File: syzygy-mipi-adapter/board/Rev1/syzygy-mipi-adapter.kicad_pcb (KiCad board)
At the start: 4 copper layers, 45 x 70 mm, 98 parts, among them J1 Conn_02x06_Odd_Even, J2 SYZYGY_STD, J3 USB_C_Receptacle_USB2.0_16P, J4 SM03B-SRSS-TB, J6 501951-2230, J7 501951-2230, J8 501951-2230, Q1 DMG1024UV-7, Q2 DMG1024UV-7, U1 RP2350_80QFN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

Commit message: Consolidate footprints from several footprint libraries into CUSTOM.pretty
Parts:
- J6, J7, J8: footprint FPC:501951-2230 -> CUSTOM:501951-2230
- L1: footprint RP2350_60QFN_minimal:L_pol_2016 -> CUSTOM:L_pol_2016
- U1: footprint RP2350_60QFN_minimal:RP2350B_QFN-80_EP_10.573x10.573_Pitch0.4mm -> CUSTOM:RP2350B_QFN-80_EP_10.573x10.573_Pitch0.4mm
- U10, U3, U4, U5, U6, U7, U8, U9: footprint FPC:PUSB3F96X -> CUSTOM:PUSB3F96X

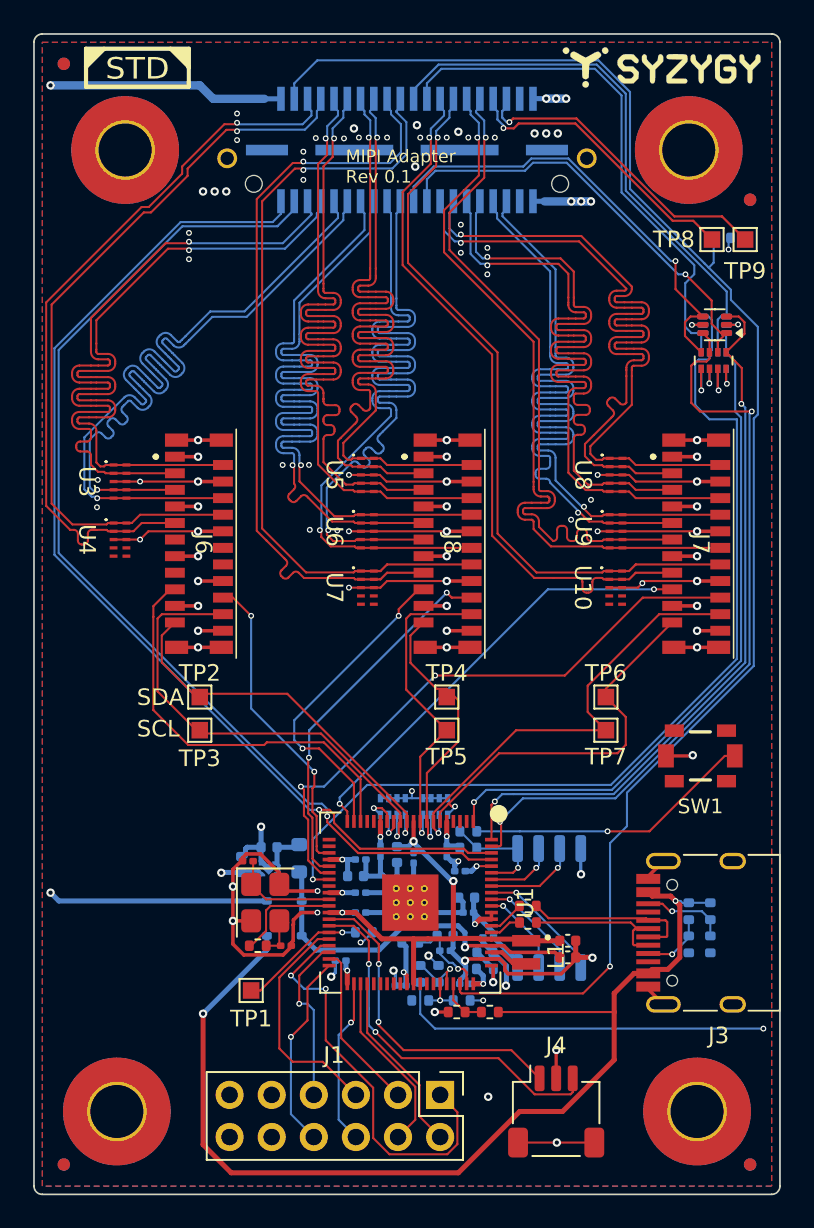
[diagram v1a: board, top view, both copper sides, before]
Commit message: Fix issue #5 as described in that issue
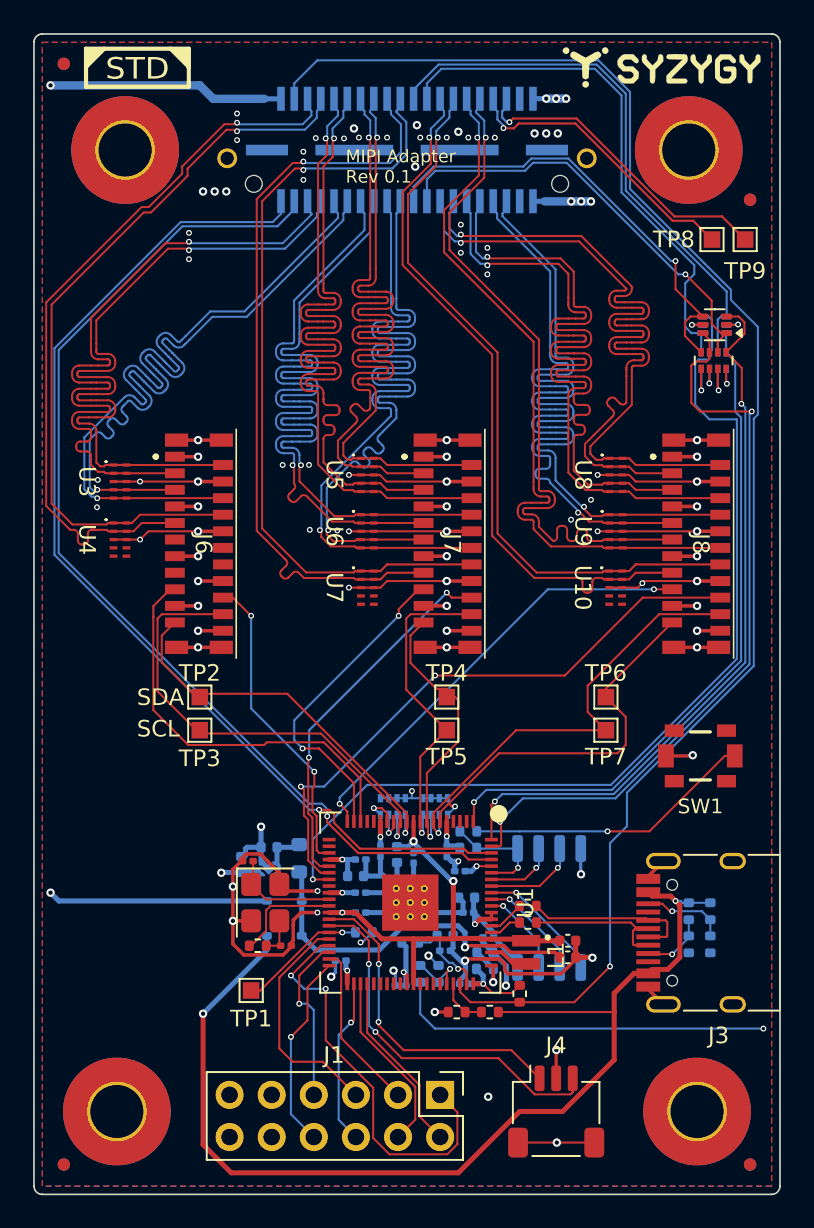
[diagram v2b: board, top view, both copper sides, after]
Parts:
- removed R10: 10K, Resistor_SMD:R_0402_1005Metric
- removed R11: 56K, Resistor_SMD:R_0402_1005Metric
- R18: moved to F.Cu
- moved R18 47.2 mm to (129.3, 117.9), turned to 90 degrees
- renumbered J8 to J7, J7 to J8
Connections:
- R18 pad 2: P3V3D -> PMCUD
- U1 pad 55: Net-(U1-GPIO44_ADC4) -> unconnected-(U1-GPIO44_ADC4-Pad55)
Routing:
- net PMCUD: track 28.8 -> 31.4 mm
- net Net-(U1-GPIO44_ADC4): track 2.48 -> 0.00 mm, vias 1 -> 0
- net P3V3D: track 16.1 -> 14.5 mm, vias 11 -> 9
- net /R_GA: track 94.9 -> 93.4 mm

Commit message: Fix issue #7
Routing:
- net P5VD: track 27.5 -> 32.8 mm
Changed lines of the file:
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@@
 	)
 	(via
-		(at 101 63.1)
+		(at 101 72.4)
 		(size 0.508)
 		(drill 0.254)
@@
 	)
 	(segment
-		(start 110.81 63.91)
-		(end 110 63.1)
+		(start 113.9 63.91)
+		(end 110.69 63.91)
 		(width 0.508)
 		(layer "B.Cu")
@@
 	)
 	(segment
-		(start 110 63.1)
-		(end 101 63.1)
+		(start 110.69 63.91)
+		(end 109.9 64.7)
+		(width 0.508)
+		(layer "B.Cu")
+		(net 1)
+	)
+	(segment
+		(start 109.9 64.7)
+		(end 109.9 68.4)
 		(width 0.508)
 		(layer "B.Cu")
@@
 	)
 	(segment
-		(start 113.9 63.91)
-		(end 110.81 63.91)
+		(start 109.9 68.4)
+		(end 105.9 72.4)
 		(width 0.508)
 		(layer "B.Cu")
+		(net 1)
+	)
+	(segment
+		(start 105.9 72.4)
+		(end 101 72.4)
+		(width 0.508)
+		(layer "B.Cu")

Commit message: Fix issue #6 and other silkscreen issues. Moved I2C test points a bit further away from FPCs.
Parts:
- moved TP4 5.81 mm to (119.1, 99.6)
- moved TP5 5.81 mm to (119.1, 101.6)
- moved TP2 5.32 mm to (115.3, 99.6)
- moved TP3 5.32 mm to (115.3, 101.6)
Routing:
- net /SCL1: track 20.1 -> 24.9 mm
- net /SDA1: track 17.0 -> 18.6 mm
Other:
- board text added: "MIPI Adapter Rev 1"
- board text added: "MIPI0"
- board text added: "MIPI1"
- board text added: "MIPI2"
- board text removed: "MIPI Adapter Rev 0.1"
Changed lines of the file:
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@@
 			(at 0.2 -1.8 270)
 			(layer "F.SilkS")
+			(hide yes)
 			(effects
 				(font
@@
 			(unlocked yes)
 			(layer "F.SilkS")
+			(hide yes)
 			(effects
 				(font
@@
 			(unlocked yes)
 			(layer "F.SilkS")
+			(hide yes)
 			(effects
 				(font
@@
 			(unlocked yes)
 			(layer "F.SilkS")
+			(hide yes)
 			(effects
 				(font
@@
 		(at 124.725 90.75 -90)
 		(property "Reference" "J7"
-			(at 0 -0.5 270)
+			(at -8.65 2.725 0)
 			(unlocked yes)
 			(layer "F.SilkS")
@@
 			(at 0 -6.95 270)
 			(layer "F.SilkS")
+			(hide yes)
 			(effects
 				(font
@@
 			(unlocked yes)
 			(layer "F.SilkS")
+			(hide yes)
 			(effects
 				(font
@@
 	(footprint "TestPoint:TestPoint_Pad_1.0x1.0mm"
 		(layer "F.Cu")
-		(at 110 102)
+		(at 115.3 101.6)
 		(descr "SMD rectangular pad as test Point, square 1.0mm side length")
 		(tags "test point SMD pad rectangle square")
@@
 		(at 109.725 90.75 -90)
 		(property "Reference" "J6"
-			(at 0 -0.5 270)
+			(at -8.65 2.725 0)
 			(unlocked yes)
 			(layer "F.SilkS")
@@
 			(unlocked yes)
 			(layer "F.SilkS")
+			(hide yes)
 			(effects
 				(font
@@
 			(unlocked yes)
 			(layer "F.SilkS")
+			(hide yes)
 			(effects
 				(font
@@
 	(footprint "TestPoint:TestPoint_Pad_1.0x1.0mm"
 		(layer "F.Cu")
-		(at 124.9 102)
+		(at 119.1 101.6)
 		(descr "SMD rectangular pad as test Point, square 1.0mm side length")
 		(tags "test point SMD pad rectangle square")
@@
 	(footprint "TestPoint:TestPoint_Pad_1.0x1.0mm"
 		(layer "F.Cu")
-		(at 110 100)
+		(at 115.3 99.6)
 		(descr "SMD rectangular pad as test Point, square 1.0mm side length")
 		(tags "test point SMD pad rectangle square")
@@
 	(footprint "TestPoint:TestPoint_Pad_1.0x1.0mm"
 		(layer "F.Cu")
-		(at 124.9 100)
+		(at 119.1 99.6)
 		(descr "SMD rectangular pad as test Point, square 1.0mm side length")
 		(tags "test point SMD pad rectangle square")
@@
 		(at 139.725 90.75 -90)
 		(property "Reference" "J8"
-			(at 0 -0.5 270)
+			(at -8.65 2.725 0)
 			(unlocked yes)
 			(layer "F.SilkS")
@@
 			(unlocked yes)
 			(layer "F.SilkS")
+			(hide yes)
 			(effects
 				(font
@@
 			(unlocked yes)
 			(layer "F.SilkS")
+			(hide yes)
 			(effects
 				(font
@@
 		(layer "Edge.Cuts")
 	)
-	(gr_text "MIPI Adapter\nRev 0.1"
+	(gr_text "MIPI Adapter\nRev 1"
 		(at 118.8 68 0)
 		(layer "F.SilkS")
@@
 		)
 	)
+	(gr_text "MIPI1"
+		(at 124.2 82.6 0)
+		(layer "F.SilkS")
+		(effects
+			(font
+				(size 1 1)
+				(thickness 0.15)
+			)
+			(justify left bottom)
+		)
+	)
 	(gr_text "SCL"
-		(at 106.2 102.5 0)
+		(at 111.2 102.2 0)
+		(layer "F.SilkS")
+		(effects
+			(font
+				(size 1 1)
+				(thickness 0.15)
+			)
+			(justify left bottom)
+		)
+	)
+	(gr_text "MIPI2"
+		(at 139.2 82.7 0)
 		(layer "F.SilkS")
 		(effects
@@
 	)
 	(gr_text "SDA"
-		(at 106.2 100.6 0)
+		(at 111.2 100.3 0)
+		(layer "F.SilkS")
+		(effects
+			(font
+				(size 1 1)
+				(thickness 0.15)
+			)
+			(justify left bottom)
+		)
+	)
+	(gr_text "MIPI0"
+		(at 109.2 82.7 0)
 		(layer "F.SilkS")
 		(effects
@@
 	)
 	(segment
-		(start 110 99.8)
-		(end 109.6 99.8)
-		(width 0.127)
-		(layer "F.Cu")
-		(net 30)
-	)
-	(segment
 		(start 122.5 107.5035)
 		(end 122.5 107.025876)
@@
 	)
 	(segment
+		(start 107.7085 97.9085)
+		(end 109.4 99.6)
+		(width 0.127)
+		(layer "F.Cu")
+		(net 30)
+	)
+	(segment
 		(start 122.5 107.5035)
 		(end 122.5 107.0205)
@@
 	)
 	(segment
-		(start 115.2795 99.8)
-		(end 110 99.8)
-		(width 0.127)
-		(layer "F.Cu")
-		(net 30)
-	)
-	(segment
 		(start 122.5 107.5035)
 		(end 122.5 108.1)
@@
 	)
 	(segment
-		(start 109.6 99.8)
-		(end 107.7085 97.9085)
+		(start 109.4 99.6)
+		(end 115.3 99.6)
 		(width 0.127)
 		(layer "F.Cu")
@@
 	)
 	(segment
+		(start 107.4535 99.6535)
+		(end 109.4 101.6)
+		(width 0.127)
+		(layer "F.Cu")
+		(net 31)
+	)
+	(segment
 		(start 121.9 108.4)
 		(end 122.0015 108.2985)
@@
 	)
 	(segment
-		(start 111.4 95)
-		(end 107.717 95)
+		(start 122.1 107.5035)
+		(end 122.1 106.9865)
 		(width 0.127)
 		(layer "F.Cu")
@@
 	)
 	(segment
-		(start 122.1 106.9865)
-		(end 117.3135 102.2)
+		(start 111.4 95)
+		(end 107.717 95)
 		(width 0.127)
 		(layer "F.Cu")
@@
 	)
 	(segment
-		(start 122.1 107.5035)
-		(end 122.1 106.9865)
+		(start 109.4 101.6)
+		(end 115.3 101.6)
 		(width 0.127)
 		(layer "F.Cu")
@@
 	)
 	(segment
-		(start 122.0015 107.602)
-		(end 122.1 107.5035)
+		(start 122.1 106.9865)
+		(end 116.7135 101.6)
 		(width 0.127)
 		(layer "F.Cu")
@@
 	)
 	(segment
-		(start 107.717 95)
-		(end 107.4535 95.2635)
+		(start 122.0015 107.602)
+		(end 122.1 107.5035)
 		(width 0.127)
 		(layer "F.Cu")
@@
 	)
 	(segment
-		(start 117.3135 102.2)
-		(end 110 102.2)
+		(start 107.717 95)
+		(end 107.4535 95.2635)
 		(width 0.127)
 		(layer "F.Cu")
@@
 	)
 	(segment
-		(start 107.4535 99.6535)
-		(end 110 102.2)
+		(start 116.7135 101.6)
+		(end 115.3 101.6)
 		(width 0.127)
 		(layer "F.Cu")
@@
 	)
 	(segment
-		(start 122.7085 96.2915)
+		(start 123.2 95.5)
 		(end 123.5 95.5)
 		(width 0.127)
@@
 	)
 	(segment
-		(start 122.7085 97.9355)
-		(end 124.273 99.5)
+		(start 123.7 103.6)
+		(end 119.7 99.6)
 		(width 0.127)
 		(layer "F.Cu")
@@
 	)
 	(segment
-		(start 124.273 99.5)
-		(end 124.9 99.5)
+		(start 119.7 99.6)
+		(end 119.1 99.6)
 		(width 0.127)
 		(layer "F.Cu")
@@
 	)
 	(segment
-		(start 125.5915 100.1915)
-		(end 124.9 99.5)
-		(width 0.127)
-		(layer "F.Cu")
-		(net 33)
-	)
-	(segment
-		(start 123.7 104.583)
-		(end 125.5915 102.6915)
-		(width 0.127)
-		(layer "F.Cu")
-		(net 33)
-	)
-	(segment
-		(start 125.5915 102.6915)
-		(end 125.5915 100.1915)
-		(width 0.127)
-		(layer "F.Cu")
-		(net 33)
-	)
-	(segment
 		(start 123.7 107.5035)
-		(end 123.7 104.583)
+		(end 123.7 103.6)
 		(width 0.127)
 		(layer "F.Cu")
@@
 	)
 	(segment
-		(start 122.7085 96.2915)
-		(end 122.7085 97.9355)
+		(start 123.7693 108.290154)
+		(end 123.907671 108.428525)
 		(width 0.127)
 		(layer "F.Cu")
@@
 	)
 	(segment
-		(start 123.7693 108.290154)
-		(end 123.907671 108.428525)
+		(start 119.1 99.6)
+		(end 123.2 95.5)
 		(width 0.127)
 		(layer "F.Cu")
@@
 	)
 	(segment
-		(start 122.453501 95.263499)
-		(end 122.453501 99.553501)
+		(start 122.717 95)
+		(end 126.4 95)
 		(width 0.127)
 		(layer "F.Cu")
@@
 	)
 	(segment
+		(start 119.1 101.6)
+		(end 117.7 100.2)
+		(width 0.127)
+		(layer "F.Cu")
+		(net 35)
+	)
+	(segment
+		(start 117.7 100.2)
+		(end 117.7 98.5)
+		(width 0.127)
+		(layer "F.Cu")
+		(net 35)
+	)
+	(segment
 		(start 123.3 103.6)
 		(end 123.3 107.5035)
@@
 	)
 	(segment
-		(start 122.453501 95.263499)
-		(end 122.717 95)
+		(start 123.3 108.1)
+		(end 123.4 108.2)
 		(width 0.127)
 		(layer "F.Cu")
@@
 	)
 	(segment
-		(start 122.453501 99.553501)
-		(end 124.9 102)
+		(start 123.3 103.6)
+		(end 121.3 101.6)
 		(width 0.127)
 		(layer "F.Cu")
@@
 	)
 	(segment
-		(start 124.9 102)
-		(end 123.3 103.6)
+		(start 121.3 101.6)
+		(end 119.1 101.6)
 		(width 0.127)
 		(layer "F.Cu")
@@
 	)
 	(segment
-		(start 123.3 108.1)
-		(end 123.4 108.2)
+		(start 119.417 98.3)
+		(end 122.717 95)
 		(width 0.127)
 		(layer "F.Cu")
@@
 	)
 	(segment
-		(start 122.717 95)
-		(end 126.4 95)
+		(start 117.7 98.5)
+		(end 117.9 98.3)
+		(width 0.127)
+		(layer "F.Cu")
+		(net 35)
+	)
+	(segment
+		(start 117.9 98.3)
+		(end 119.417 98.3)
 		(width 0.127)
 		(layer "F.Cu")
